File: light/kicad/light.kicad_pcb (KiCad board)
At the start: 2 copper layers, 30 x 30 mm, 111 parts, among them U1 FT4232H, U11 TLV7103318DDSE, U14 74LVC1G07, U2 SN74AVC4T774RSVR, U3 SN74AVC4T774RSVR, U4 SN74AVC4T774RSVR, U5 74LVC1G07, U6 SN74AHC595QWBQBRQ1, U7 TLV75533PDBV, U8 TLV75533PDBV, U9 93LC56BT-I/OT, Y1 12MHz_7M-12.000MAAJ

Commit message: kicad: add notes and update PCB file
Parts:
- removed R15, R23, R24: 0, Resistor_SMD:R_0603_1608Metric
- removed TP1, TP10, TP11, TP12, TP13, TP14, TP15, TP16, TP17, TP18, TP19, TP2, TP3, TP4, TP5, TP6, TP7, TP8, TP9: TestPoint, TestPoint:TestPoint_Pad_D1.5mm
- added ADBUS5: TestPoint, TestPoint:TestPoint_Pad_D1.5mm, F.Cu at (231.5, 81.5)
- added BD_BUS6: TestPoint, TestPoint:TestPoint_Pad_D1.5mm, F.Cu at (231.5, 84.0)
- added CDBUS3: TestPoint, TestPoint:TestPoint_Pad_D1.5mm, F.Cu at (231.5, 86.5)
- added CDBUS5: TestPoint, TestPoint:TestPoint_Pad_D1.5mm, F.Cu at (231.5, 89.0)
- added DDBUS2: TestPoint, TestPoint:TestPoint_Pad_D1.5mm, F.Cu at (231.5, 91.5)
- added DDBUS4: TestPoint, TestPoint:TestPoint_Pad_D1.5mm, F.Cu at (231.5, 94.0)
- added R35: 0, Resistor_SMD:R_0603_1608Metric, F.Cu at (252.5, 119.7)
- added R36: 0, Resistor_SMD:R_0603_1608Metric, F.Cu at (249.5, 119.7)
- C1, C15, C17, C18, C19, C2, C22, C23, C24, C25, C27, C28, C3, C4, C5, C6, C7, C8, C9: footprint Capacitor_SMD:C_0603_1608Metric -> Capacitor_SMD:C_0201_0603Metric
- C10, C13, C14, C16, C26, C29, C30: footprint Capacitor_SMD:C_0603_1608Metric -> Capacitor_SMD:C_0201_0603Metric; moved to F.Cu
- C11, C12: footprint Capacitor_SMD:C_0603_1608Metric -> Capacitor_SMD:C_0201_0603Metric; moved to B.Cu
- L1, L2, R10, R11, R12, R13, R14, R7, R8, R9, U7: moved to B.Cu
- R1, R20, R25, R26, R27, R28: footprint Resistor_SMD:R_0603_1608Metric -> Resistor_SMD:R_0402_1005Metric
- R16, R17, R18, R21, R29, R31, R5, R6: footprint Resistor_SMD:R_0603_1608Metric -> Resistor_SMD:R_0201_0603Metric
- R2, R3: footprint Resistor_SMD:R_0603_1608Metric -> Resistor_SMD:R_0402_1005Metric; moved to F.Cu
- R32, R4: footprint Resistor_SMD:R_0603_1608Metric -> Resistor_SMD:R_0201_0603Metric; moved to F.Cu
- moved Y1 145.8 mm to (250.5, 114.0), turned to 180 degrees
- moved C27 143.3 mm to (251.1, 111.7), turned to 180 degrees
- moved LED5 141.9 mm to (243.0, 119.8)
- moved C28 141.7 mm to (249.6, 111.7)
- moved L2 139.4 mm to (249.0, 109.0)
- moved C12 138.3 mm to (249.0, 107.5), turned to 90 degrees
- moved C13 138.3 mm to (249.0, 107.5), turned to 90 degrees
- moved R33 138.1 mm to (251.0, 119.7)
- moved R5 137.0 mm to (236.8, 96.0)
- moved LED6 135.9 mm to (238.5, 119.8)
- moved HOST1 135.8 mm to (249.1, 124.7)
- moved LED3 135.8 mm to (240.0, 119.8)
- moved LED4 135.7 mm to (241.5, 119.8)
- moved C5 135.1 mm to (246.1, 108.5)
- moved R9 134.8 mm to (236.0, 116.8), turned to 90 degrees
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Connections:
- net /FTDI_RX_EC_TX_CONN renamed /DUT_CCD_SBU2
- net /FTDI_TX_EC_RX_CONN renamed /DUT_CCD_SBU1
- net /JTAG_TDI renamed /EC_JTAG_TDI
- JDB11 pad 1: Net-(JDB11-VTref) -> EC_VREF
- JDB11 pad 2: /JTAG_TMS -> /EC_JTAG_TMS
- JDB11 pad 4: /JTAG_TCK -> /EC_JTAG_TCK
- JDB11 pad 6: /JTAG_TDO -> /EC_JTAG_TDO
- JPD1 pad 1: /PD_VREF -> unconnected-(JPD1-Pad1)
- JPD1 pad 2: GND -> /PD_SWDIO
- JPD1 pad 3: /PD_XRES -> /PD_SWCLK
- JPD1 pad 4: /PD_SWCLK -> /PD_XRES
- JPD1 pad 5: /PD_SWDIO -> GND
- JPD1 pad 6: unconnected-(JPD1-Pad6) -> /PD_VREF
- JSPI1 pad 1: GND -> AP_SPI_VREF
- JSPI1 pad 2: /AP_SPI_CLK -> /AP_SPI_CS
- JSPI1 pad 3: /AP_SPI_D1 -> /AP_SPI_MISO_D0
- JSPI1 pad 4: /AP_SPI_D0 -> /AP_SPI_MOSI_D1
- JSPI1 pad 5: /AP_SPI_CS -> /AP_SPI_CLK
- JSPI1 pad 6: AP_SPI_VREF -> GND
- R21 pad 2: /JTAG_TDO -> /EC_JTAG_TDO
- U1 pad 23: Net-(U1-ADBUS6) -> unconnected-(U1-ADBUS6-Pad23)
- U1 pad 24: Net-(U1-ADBUS7) -> unconnected-(U1-ADBUS7-Pad24)
- U1 pad 36: Net-(U1-~{SUSPEND}) -> unconnected-(U1-~{SUSPEND}-Pad36)
- U1 pad 45: Net-(U1-CDBUS6) -> unconnected-(U1-CDBUS6-Pad45)
- U1 pad 46: Net-(U1-CDBUS7) -> unconnected-(U1-CDBUS7-Pad46)
- U1 pad 54: Net-(U1-DDBUS3) -> unconnected-(U1-DDBUS3-Pad54)
- U1 pad 57: Net-(U1-DDBUS5) -> unconnected-(U1-DDBUS5-Pad57)
- U1 pad 58: Net-(U1-DDBUS6) -> unconnected-(U1-DDBUS6-Pad58)
- U1 pad 59: Net-(U1-DDBUS7) -> unconnected-(U1-DDBUS7-Pad59)
- U2 pad 10: /AP_SPI_D0 -> /AP_SPI_MISO_D0
- U2 pad 11: /AP_SPI_D1 -> /AP_SPI_MOSI_D1
- U3 pad 10: /JTAG_TDO -> /EC_JTAG_TDO
- U3 pad 12: /JTAG_TCK -> /EC_JTAG_TCK
- U3 pad 9: /JTAG_TMS -> /EC_JTAG_TMS
- U6 pad 1: Net-(U6-QB) -> unconnected-(U6-QB-Pad1)
- U6 pad 3: Net-(U6-QD) -> unconnected-(U6-QD-Pad3)
- U6 pad 9: Net-(U6-QH') -> unconnected-(U6-QH&apos;-Pad9)
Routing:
- net CCD_VBUS: track 0.00 -> 3.21 mm
- net Net-(U1-CDBUS3): vias 0 -> 1
- net GND: vias 1 -> 0
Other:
- board size 30 x 30 mm -> 24 x 55.9 mm

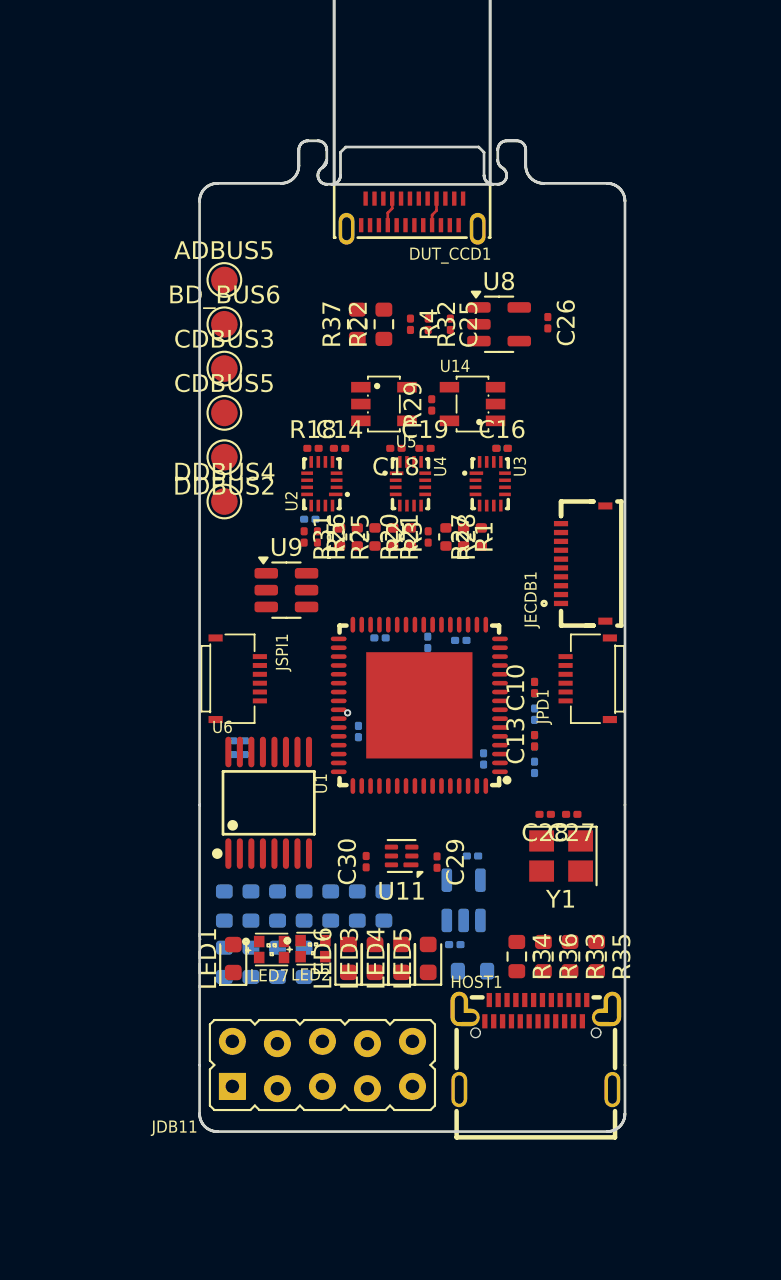
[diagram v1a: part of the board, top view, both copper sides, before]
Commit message: kidcad: feedback implementation and updating boardfile version
12/16

1. Add a jumper for forcing power on to target device (J1)
2. add pull down on enable pins of FTDI. e.g. U11 (R15, R23)
3. add SPI Socket footprint  (TBD)
4. Add CC2 5.1k of Host connector (R24)
5. add pin header for EC Reset (J2)
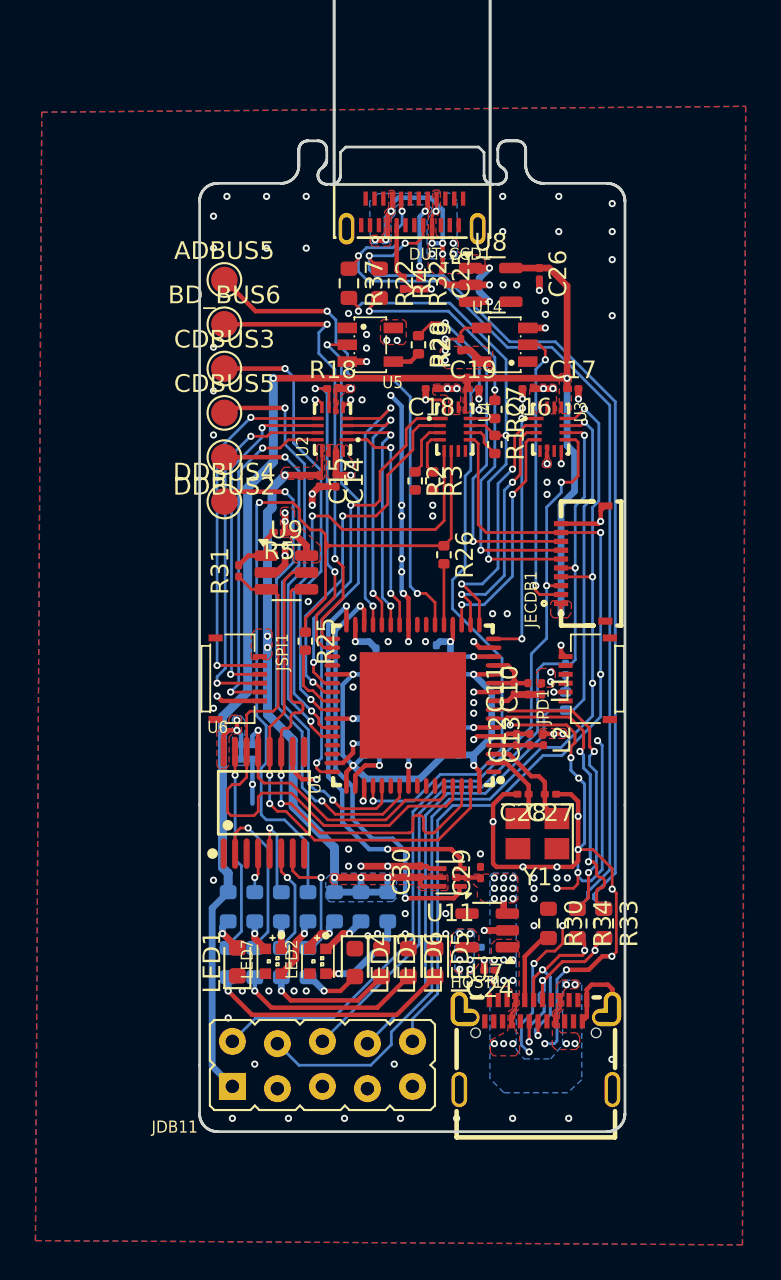
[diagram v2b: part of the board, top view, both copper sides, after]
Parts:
- C11, C12, C15, C17, C24, L1, L2, R30, U7: moved to F.Cu
- R20, R21, R35, R36: moved to B.Cu
- moved R20 12.7 mm to (250.7, 105.3), turned to -90 degrees
- moved R28 11.0 mm to (242.5, 85.2)
- moved R21 10.8 mm to (250.7, 103.5)
- moved R27 7.23 mm to (246.8, 88.8), turned to -90 degrees
- moved R25 6.19 mm to (236.1, 101.9)
- moved R1 5.51 mm to (246.8, 90.8)
- moved C17 5.22 mm to (251.2, 87.6)
- moved C23 5.15 mm to (245.6, 119.2), turned to 0 degrees
- moved R30 5.06 mm to (249.8, 117.8), turned to -90 degrees
- moved R26 4.99 mm to (243.9, 97.0), turned to -90 degrees
- moved U3 4.60 mm to (249.9, 89.9)
- moved C19 4.33 mm to (245.5, 87.6)
- moved R10 4.29 mm to (231.7, 120.0)
- moved R31 4.16 mm to (232.3, 97.9), turned to 90 degrees
- moved U4 3.97 mm to (244.5, 89.9)
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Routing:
- net GND: track 0.00 -> 126.8 mm, vias 0 -> 127
- net EC_VREF: track 0.00 -> 84.0 mm, vias 0 -> 3
- net /EC_JTAG_TCK: track 0.00 -> 53.5 mm, vias 0 -> 3
- net /DUT_CCD_SBU2: track 0.00 -> 53.5 mm, vias 0 -> 2
- net /DUT_CCD_SBU1: track 0.00 -> 52.2 mm, vias 0 -> 2
- net /EC_RST_UNSHIFTED: track 0.00 -> 47.8 mm, vias 0 -> 1
- net /EC_JTAG_TMS: track 0.00 -> 47.5 mm, vias 0 -> 2
- net /~{EC_RST}: track 0.00 -> 47.3 mm, vias 0 -> 2
- net /EC_JTAG_TDO: track 0.00 -> 44.4 mm, vias 0 -> 2
- net /EC_JTAG_TDI: track 0.00 -> 43.7 mm, vias 0 -> 1
- net AP_SPI_VREF: track 0.00 -> 41.0 mm, vias 0 -> 6
- net /FTDI_RX_AP_TX_UNSHIFTED: track 0.00 -> 37.8 mm, vias 0 -> 2
- net /EEDATA: track 0.00 -> 33.0 mm
- net 3.3V: track 0.00 -> 30.7 mm, vias 0 -> 32
- net /FTDI_RX_EC_TX: track 0.00 -> 29.0 mm, vias 0 -> 3
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- added copper zone on B.Cu, net 3.3V
- added copper zone on F.Cu, net 3.3V
- added copper zone on In2.Cu, net 3.3V
- added copper zone on B.Cu, net AP_SPI_VREF
- added copper zone on F.Cu, net AP_SPI_VREF
- added copper zone on B.Cu, net CCD_VBUS
- added copper zone on F.Cu, net CCD_VBUS
- added copper zone on In2.Cu, net CCD_VBUS
- added copper zone on F.Cu, net EC_VREF
- added copper zone on B.Cu, net GND
- added copper zone on F.Cu, net GND
- added copper zone on In1.Cu, net GND
- added copper zone on B.Cu, net HOST_VBUS
- added copper zone on F.Cu, net HOST_VBUS
- added copper zone on In2.Cu, net HOST_VBUS
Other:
- copper layers 2 -> 4

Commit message: kicad: add footprints and upload new placement
1. change JDB11 package footprint
2.  add footrprint for J3
3.  Change U6 footprint to WQFN
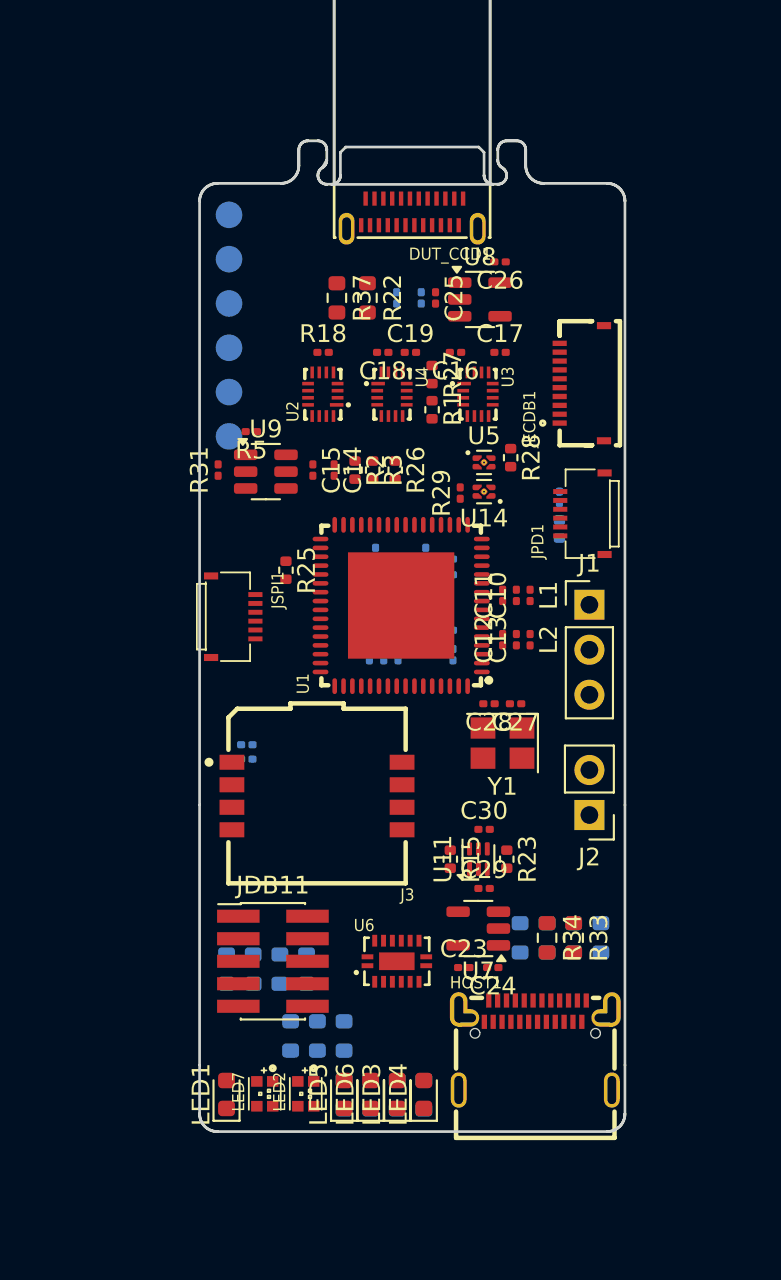
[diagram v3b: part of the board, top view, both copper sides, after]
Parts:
- added J1: Conn_01x03_Pin, Connector_PinHeader_2.54mm:PinHeader_1x03_P2.54mm_Vertical, F.Cu at (252.1, 99.8)
- added J2: Conn_01x02_Pin, Connector_PinHeader_2.54mm:PinHeader_1x02_P2.54mm_Vertical, F.Cu at (252.1, 111.7)
- added J3: SPI Socket, 0JLC:50950-0084N-002, F.Cu at (236.7, 110.6)
- added R15: 100k, Resistor_SMD:R_0402_1005Metric, F.Cu at (244.2, 114.2)
- added R23: 100k, Resistor_SMD:R_0402_1005Metric, F.Cu at (247.4, 114.2)
- added R24: 5.1k, Resistor_SMD:R_0603_1608Metric, B.Cu at (248.2, 118.6)
- ADBUS5, BD_BUS6, CDBUS3, CDBUS5, DDBUS2, DDBUS4, R30, R32, R4: moved to B.Cu
- C23: moved to F.Cu
- JDB11: footprint Library_Myself:Conn_ARM_JTAG_SWD_10 -> Connector_PinHeader_1.27mm:PinHeader_2x05_P1.27mm_Vertical_SMD
- U14, U5: footprint Library_Myself:SOT-23-5_L3.0-W1.7-P0.95-LS2.8-BR -> Package_SON:Texas_X2SON-5_0.8x0.8mm_P0.48mm_RoutingVia
- U6: footprint Library_Myself:TSSOP-16_L5.0-W4.4-P0.65-LS6.4-BL -> 0JLC:DHVQFN-16_L3.5-W2.5-P0.50-BL-EP
- moved U6 11.7 mm to (241.2, 119.9)
- moved JECDB1 10.2 mm to (250.4, 87.3)
- moved R10 9.92 mm to (238.3, 127.5)
- moved R11 9.92 mm to (239.8, 127.5)
- moved R12 9.92 mm to (241.3, 127.5)
- moved R13 9.92 mm to (242.8, 127.5)
- moved R20 9.72 mm to (250.4, 95.5)
- moved R21 9.72 mm to (250.4, 93.8)
- moved JPD1 9.32 mm to (251.7, 94.7)
- moved U5 9.23 mm to (246.2, 91.8), turned to 0 degrees
- moved LED5 9.04 mm to (238.3, 127.5), turned to 90 degrees
- moved LED4 8.40 mm to (242.8, 127.5), turned to 90 degrees
- moved U14 8.37 mm to (246.2, 93.4), turned to 180 degrees
- moved R29 8.37 mm to (244.8, 93.5)
- moved R28 8.22 mm to (247.7, 91.5)
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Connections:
- C25 pad 1: CCD_VBUS -> Net-(J1-Pin_2)
- HOST1 pad B5: unconnected-(HOST1-CC2-PadB5) -> Net-(HOST1-CC2)
- U8 pad 1: CCD_VBUS -> Net-(J1-Pin_2)
- U8 pad 3: CCD_VBUS -> Net-(J1-Pin_2)
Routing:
- net GND: track 126.8 -> 0.00 mm, vias 127 -> 0
- net EC_VREF: track 84.0 -> 0.00 mm, vias 3 -> 0
- net /EC_JTAG_TCK: track 53.5 -> 0.00 mm, vias 3 -> 0
- net /DUT_CCD_SBU2: track 53.5 -> 0.00 mm, vias 2 -> 0
- net /DUT_CCD_SBU1: track 52.2 -> 0.00 mm, vias 2 -> 0
- net /EC_RST_UNSHIFTED: track 47.8 -> 0.00 mm, vias 1 -> 0
- net /EC_JTAG_TMS: track 47.5 -> 0.00 mm, vias 2 -> 0
- net /~{EC_RST}: track 47.3 -> 0.00 mm, vias 2 -> 0
- net /EC_JTAG_TDO: track 44.4 -> 0.00 mm, vias 2 -> 0
- net /EC_JTAG_TDI: track 43.7 -> 0.00 mm, vias 1 -> 0
- net AP_SPI_VREF: track 41.0 -> 0.00 mm, vias 6 -> 0
- net /FTDI_RX_AP_TX_UNSHIFTED: track 37.8 -> 0.00 mm, vias 2 -> 0
- net /EEDATA: track 33.0 -> 0.00 mm
- net 3.3V: track 30.7 -> 0.00 mm, vias 32 -> 0
- net /FTDI_RX_EC_TX: track 29.0 -> 0.00 mm, vias 3 -> 0
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- removed copper zone on B.Cu, net 3.3V
- removed copper zone on F.Cu, net 3.3V
- removed copper zone on In2.Cu, net 3.3V
- removed copper zone on B.Cu, net AP_SPI_VREF
- removed copper zone on F.Cu, net AP_SPI_VREF
- removed copper zone on B.Cu, net CCD_VBUS
- removed copper zone on F.Cu, net CCD_VBUS
- removed copper zone on In2.Cu, net CCD_VBUS
- removed copper zone on F.Cu, net EC_VREF
- removed copper zone on B.Cu, net GND
- removed copper zone on F.Cu, net GND
- removed copper zone on In1.Cu, net GND
- removed copper zone on B.Cu, net HOST_VBUS
- removed copper zone on F.Cu, net HOST_VBUS
- removed copper zone on In2.Cu, net HOST_VBUS

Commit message: kicad: Update board file layout routing
update board file.
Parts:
- R32, R4, R6: moved to F.Cu
- moved C22 13.0 mm to (239.4, 119.7)
- moved R6 12.5 mm to (240.6, 117.4), turned to -90 degrees
- moved C25 5.97 mm to (249.2, 81.1)
- moved C26 3.16 mm to (249.2, 82.8), turned to 90 degrees
- moved R23 3.02 mm to (245.5, 111.9), turned to 0 degrees
- moved C29 2.94 mm to (247.4, 113.1), turned to 90 degrees
- moved C30 2.51 mm to (243.7, 113.1), turned to 90 degrees
- moved R22 2.48 mm to (242.0, 82.1)
- moved R26 2.23 mm to (241.7, 90.1)
- moved R2 2.15 mm to (238.9, 90.1)
- moved R3 2.15 mm to (239.9, 90.1)
- moved C14 2.08 mm to (237.5, 90.2)
- moved C15 2.07 mm to (236.5, 90.2)
- moved R37 1.75 mm to (239.5, 82.1)
- moved L2 1.64 mm to (248.0, 103.2), turned to 90 degrees
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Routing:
- net GND: track 0.00 -> 118.1 mm, vias 0 -> 142
- net /~{EC_RST}: track 0.00 -> 67.9 mm, vias 0 -> 2
- net EC_VREF: track 0.00 -> 65.7 mm, vias 0 -> 4
- net AP_SPI_VREF: track 0.00 -> 54.7 mm, vias 0 -> 7
- net /DUT_CCD_SBU2: track 0.00 -> 54.3 mm, vias 0 -> 2
- net /EC_RST_UNSHIFTED: track 0.00 -> 52.0 mm, vias 0 -> 4
- net /EC_JTAG_TDO: track 0.00 -> 51.8 mm, vias 0 -> 4
- net /EC_JTAG_TDI: track 0.00 -> 50.9 mm, vias 0 -> 4
- net /DUT_CCD_SBU1: track 0.00 -> 49.2 mm, vias 0 -> 1
- net /EC_JTAG_TCK: track 0.00 -> 45.6 mm, vias 0 -> 3
- net /SPI_VREF_FORCE_1.8: track 0.00 -> 45.3 mm, vias 0 -> 2
- net /EC_JTAG_TMS: track 0.00 -> 44.1 mm, vias 0 -> 2
- net /SPI_VREF_FORCE_3.3: track 0.00 -> 43.1 mm, vias 0 -> 2
- net /EEDATA: track 0.00 -> 41.5 mm, vias 0 -> 3
- net /EECS: track 0.00 -> 40.9 mm, vias 0 -> 3
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- added copper zone on B.Cu, net 3.3V
- added copper zone on F.Cu, net 3.3V
- added copper zone on In2.Cu, net 3.3V
- added copper zone on B.Cu, net AP_SPI_VREF
- added copper zone on F.Cu, net AP_SPI_VREF
- added copper zone on B.Cu, net CCD_VBUS
- added copper zone on F.Cu, net CCD_VBUS
- added copper zone on In2.Cu, net CCD_VBUS
- added copper zone on B.Cu, net GND
- added copper zone on F.Cu, net GND
- added copper zone on In1.Cu, net GND
- added copper zone on B.Cu, net HOST_VBUS
- added copper zone on F.Cu, net HOST_VBUS
- added copper zone on In2.Cu, net HOST_VBUS
- added copper zone on F.Cu, net Net-(J1-Pin_2)
- added copper zone on In1.Cu, net Net-(J1-Pin_2)
